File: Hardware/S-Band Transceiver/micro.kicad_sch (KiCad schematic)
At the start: 40 parts, among them J2 AVR-UPDI-6, J4 USB_C_Receptacle_USB2.0_16P, SW1 SW_Push, U11 AVR128DA48x-xPT, U12 ADS1118IDGS, U8 FT231XQ

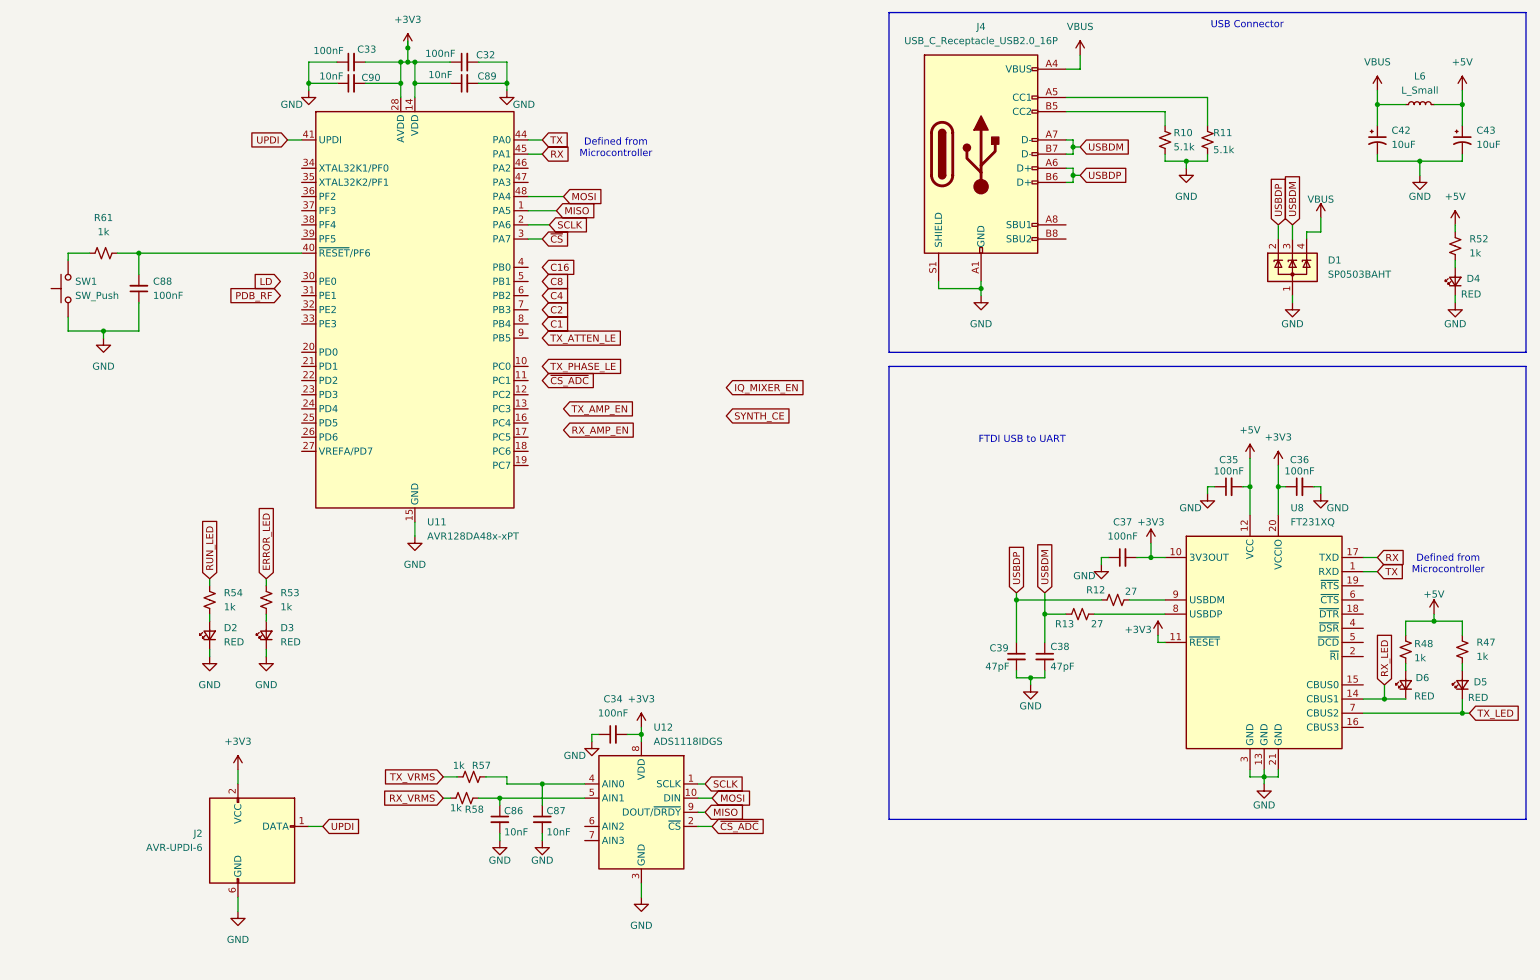
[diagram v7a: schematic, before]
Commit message: Updates to Schematic
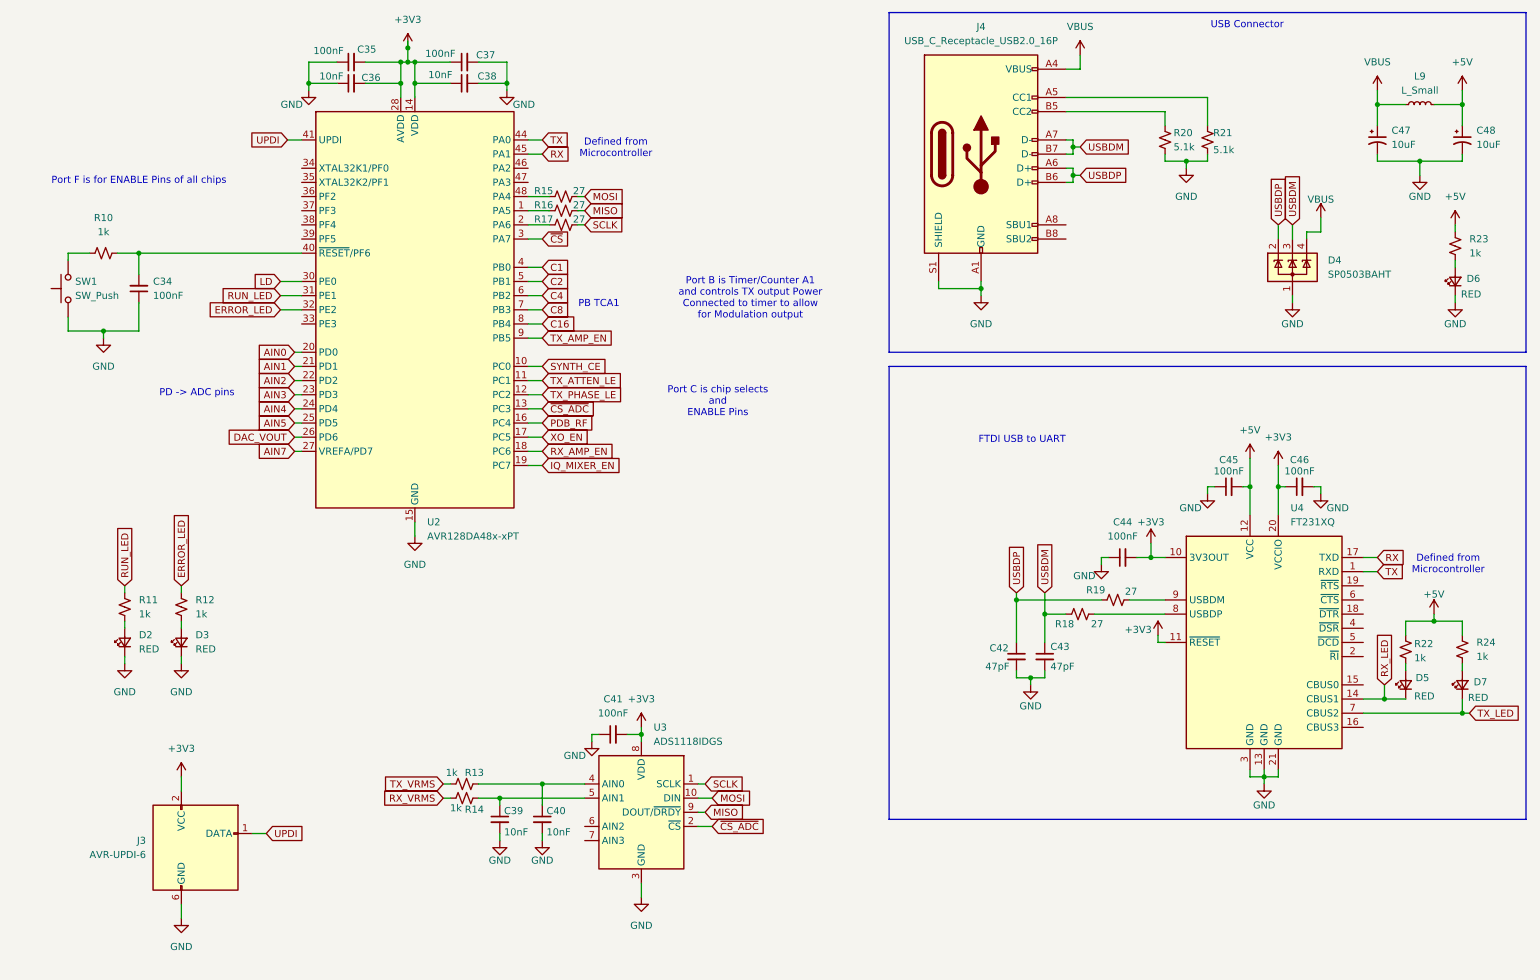
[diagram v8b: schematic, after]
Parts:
- added R15, R16, R17: 27, symbol Device:R_Small_US
- U2: renamed from U11; Digikey (none) -> 150-AVR128DA48-I/PT-ND
- U3: renamed from U12; footprint (none) -> Package_SO:MSOP-10_3x3mm_P0.5mm
- U4: renamed from U8; Digikey (none) -> 768-1128-1-ND
- renumbered C88 to C34, C33 to C35, C90 to C36, C32 to C37, C89 to C38, C86 to C39, C87 to C40, C34 to C41, C39 to C42, C38 to C43, C37 to C44, C35 to C45, C36 to C46, C42 to C47, C43 to C48, D1 to D4, D6 to D5, D4 to D6, D5 to D7, J2 to J3, L6 to L9, R61 to R10, R54 to R11, R53 to R12, R57 to R13, R58 to R14, R13 to R18, R12 to R19, R10 to R20, R11 to R21, R48 to R22, R52 to R23, R47 to R24
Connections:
- net C1: now also U2.4 (PB0)
- net C16: now also U2.8 (PB4)
- net C2: now also U2.5 (PB1)
- net C4: now also U2.6 (PB2)
- net C8: now also U2.7 (PB3)
- net ERROR_LED: now also U2.32 (PE2)
- net IQ_MIXER_EN: now also U2.19 (PC7)
- net LD: now also U2.30 (PE0)
- net MISO: now also R16.2; no longer U2.1 (PA5)
- net MOSI: now also R15.2; no longer U2.48 (PA4)
- net PDB_RF: now also U2.16 (PC4)
- net RUN_LED: now also U2.31 (PE1)
- net RX_AMP_EN: now also U2.18 (PC6)
- net SCLK: now also R17.2; no longer U2.2 (PA6)
- net SYNTH_CE: now also U2.10 (PC0)
- net TX_AMP_EN: now also U2.9 (PB5)
- net TX_ATTEN_LE: now also U2.11 (PC1)
- net TX_PHASE_LE: now also U2.12 (PC2)
- net ~{CS_ADC}: now also U2.13 (PC3)
- net XO_EN: now reaches U2.17 (PC5)
- net AIN0: now reaches U2.20 (PD0)
- net AIN1: now reaches U2.21 (PD1)
- net AIN2: now reaches U2.22 (PD2)
- net AIN3: now reaches U2.23 (PD3)
- net AIN4: now reaches U2.24 (PD4)
- net AIN5: now reaches U2.25 (PD5)
- net DAC_VOUT: now reaches U2.26 (PD6)
- net AIN7: now reaches U2.27 (VREFA/PD7)
- new net: R16.1, U2.1 (PA5)
- new net: R17.1, U2.2 (PA6)
- new net: R15.1, U2.48 (PA4)
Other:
- note added: "PB TCA1"
- note added: "PD -> ADC pins"
- note added: "Port B is Timer/Counter A1 and controls TX output Power Connected to timer to allow for Modulation output"
- note added: "Port C is chip selects and ENABLE Pins"
- note added: "Port F is for ENABLE Pins of all chips"
- moved on the sheet: D2, D3, J3, R11, R12, R13
